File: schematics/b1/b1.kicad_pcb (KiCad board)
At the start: 2 copper layers, 0 parts

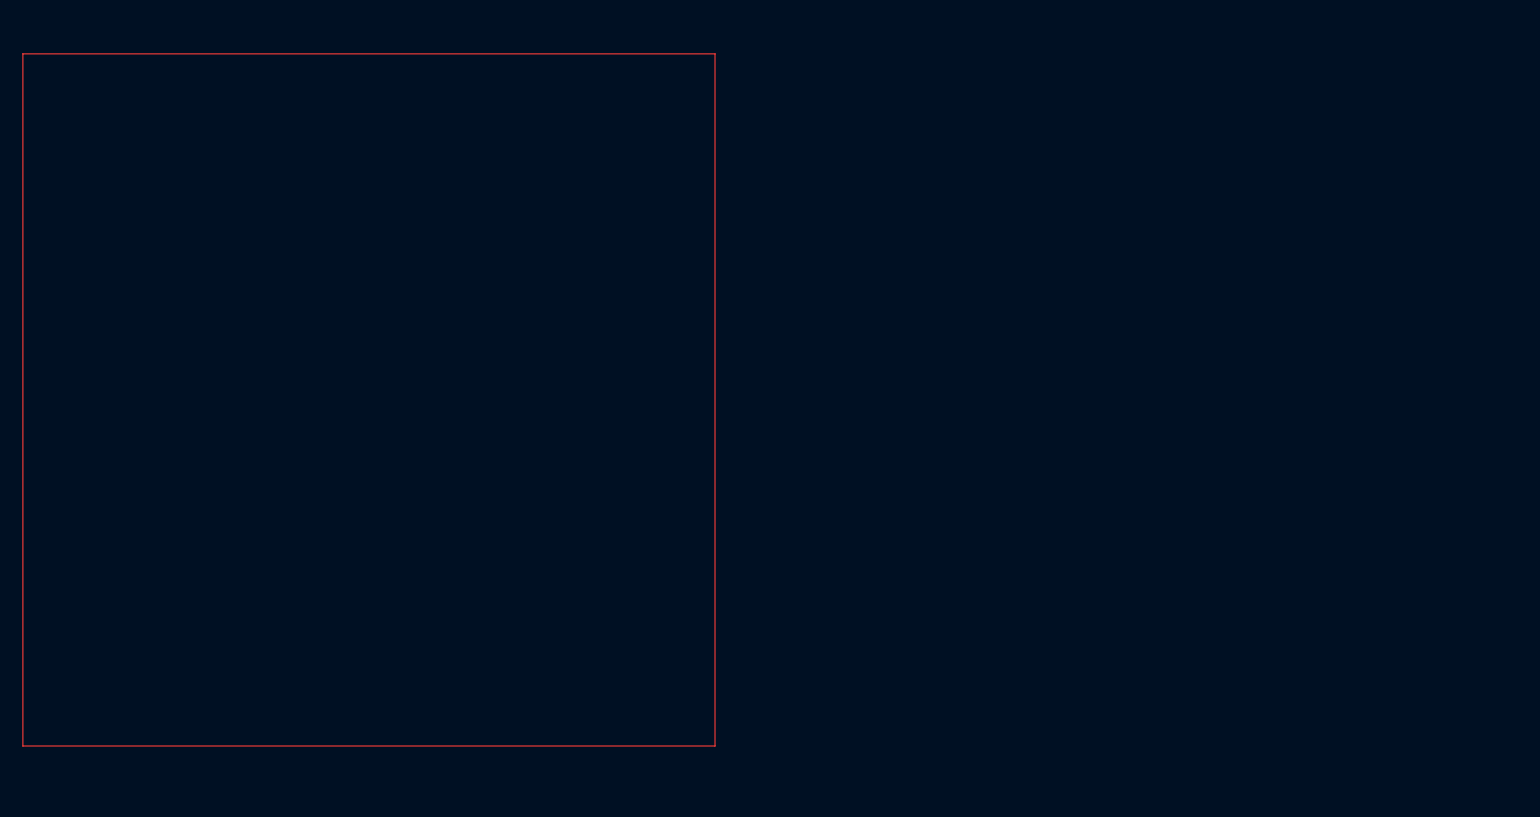
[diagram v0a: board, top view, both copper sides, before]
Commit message: Added terminal block for power in.
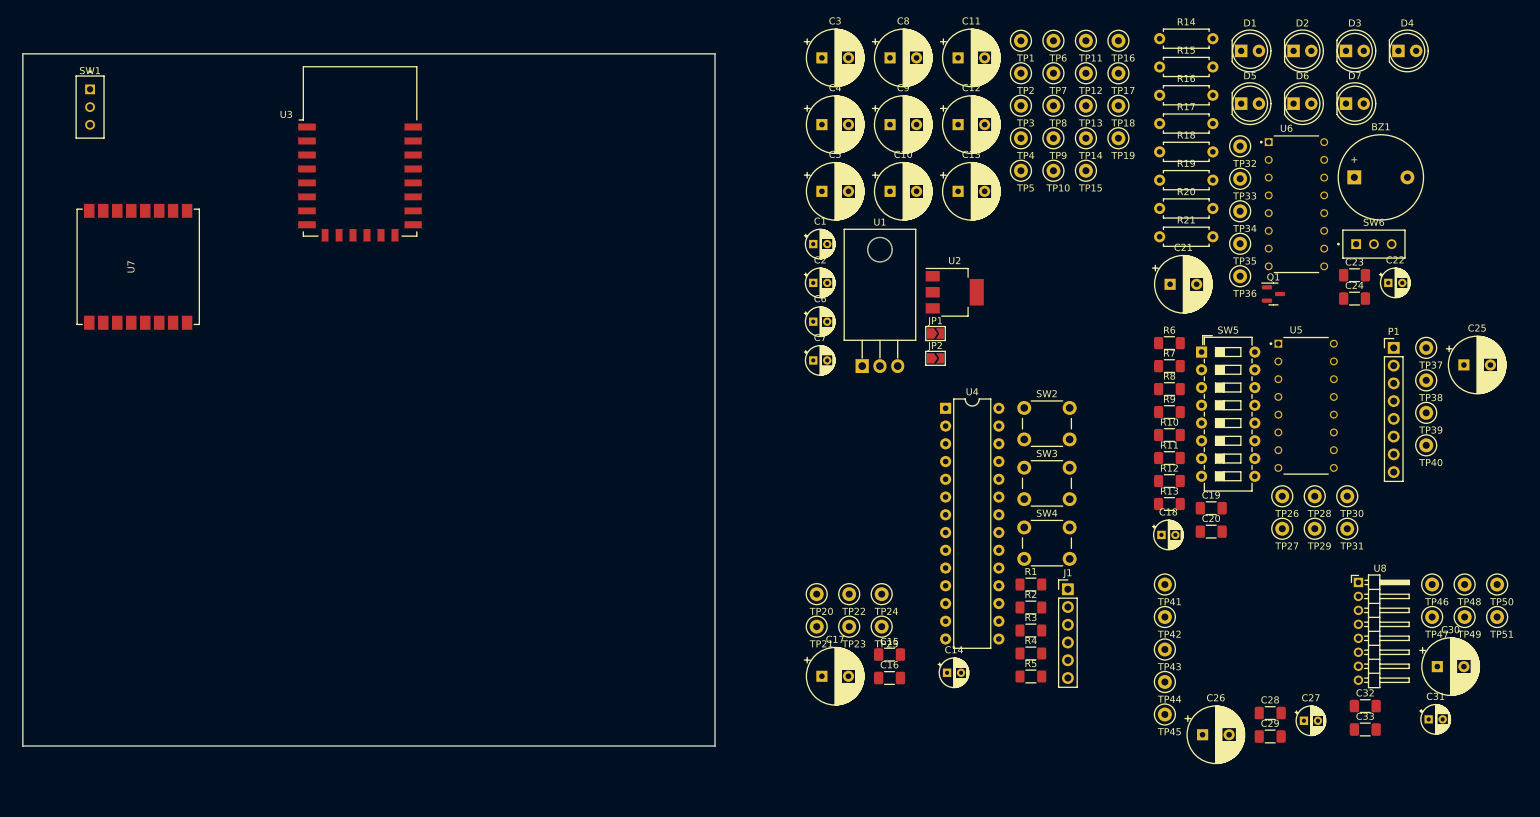
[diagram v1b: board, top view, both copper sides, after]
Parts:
- added BZ1: Buzzer, Buzzer_Beeper:Buzzer_12x9.5RM7.6, F.Cu at (285.8, 60.9)
- added C1: 10u, Capacitor_THT:CP_Radial_D4.0mm_P2.00mm, F.Cu at (208.4, 70.4)
- added C10: C, Capacitor_THT:CP_Radial_D8.0mm_P3.80mm, F.Cu at (219.4, 62.9)
- added C11: C, Capacitor_THT:CP_Radial_D8.0mm_P3.80mm, F.Cu at (229.1, 43.8)
- added C12: C, Capacitor_THT:CP_Radial_D8.0mm_P3.80mm, F.Cu at (229.1, 53.3)
- added C13: C, Capacitor_THT:CP_Radial_D8.0mm_P3.80mm, F.Cu at (229.1, 62.9)
- added C14: 10u, Capacitor_THT:CP_Radial_D4.0mm_P2.00mm, F.Cu at (227.5, 131.8)
- added C15: 1u, Capacitor_SMD:C_1206_3216Metric_Pad1.33x1.80mm_HandSolder, F.Cu at (219.3, 129.2)
- added C16: 0.1u, Capacitor_SMD:C_1206_3216Metric_Pad1.33x1.80mm_HandSolder, F.Cu at (219.3, 132.5)
- added C17: 1m, Capacitor_THT:CP_Radial_D8.0mm_P3.80mm, F.Cu at (209.6, 132.3)
- added C18: 10u, Capacitor_THT:CP_Radial_D4.0mm_P2.00mm, F.Cu at (258.2, 112.0)
- added C19: 1u, Capacitor_SMD:C_1206_3216Metric_Pad1.33x1.80mm_HandSolder, F.Cu at (265.3, 108.2)
- added C2: 10u, Capacitor_THT:CP_Radial_D4.0mm_P2.00mm, F.Cu at (208.4, 76.0)
- added C20: 0.1u, Capacitor_SMD:C_1206_3216Metric_Pad1.33x1.80mm_HandSolder, F.Cu at (265.3, 111.6)
- added C21: 470u, Capacitor_THT:CP_Radial_D8.0mm_P3.80mm, F.Cu at (259.4, 76.2)
- added C22: 10u, Capacitor_THT:CP_Radial_D4.0mm_P2.00mm, F.Cu at (290.7, 76.0)
- added C23: 1u, Capacitor_SMD:C_1206_3216Metric_Pad1.33x1.80mm_HandSolder, F.Cu at (285.8, 74.9)
- added C24: 0.1u, Capacitor_SMD:C_1206_3216Metric_Pad1.33x1.80mm_HandSolder, F.Cu at (285.8, 78.2)
- added C25: 1m, Capacitor_THT:CP_Radial_D8.0mm_P3.80mm, F.Cu at (301.5, 87.7)
- added C26: 1m, Capacitor_THT:CP_Radial_D8.0mm_P3.80mm, F.Cu at (264.1, 140.6)
- added C27: 10u, Capacitor_THT:CP_Radial_D4.0mm_P2.00mm, F.Cu at (278.6, 138.6)
- added C28: 1u, Capacitor_SMD:C_1206_3216Metric_Pad1.33x1.80mm_HandSolder, F.Cu at (273.8, 137.5)
- added C29: 0.1u, Capacitor_SMD:C_1206_3216Metric_Pad1.33x1.80mm_HandSolder, F.Cu at (273.8, 140.9)
- added C3: C, Capacitor_THT:CP_Radial_D8.0mm_P3.80mm, F.Cu at (209.6, 43.8)
- added C30: 470u, Capacitor_THT:CP_Radial_D8.0mm_P3.80mm, F.Cu at (297.7, 130.9)
- added C31: 10u, Capacitor_THT:CP_Radial_D4.0mm_P2.00mm, F.Cu at (296.4, 138.4)
- added C32: 1u, Capacitor_SMD:C_1206_3216Metric_Pad1.33x1.80mm_HandSolder, F.Cu at (287.4, 136.5)
- added C33: 0.1u, Capacitor_SMD:C_1206_3216Metric_Pad1.33x1.80mm_HandSolder, F.Cu at (287.4, 139.9)
- added C4: C, Capacitor_THT:CP_Radial_D8.0mm_P3.80mm, F.Cu at (209.6, 53.3)
- added C5: C, Capacitor_THT:CP_Radial_D8.0mm_P3.80mm, F.Cu at (209.6, 62.9)
- added C6: 10u, Capacitor_THT:CP_Radial_D4.0mm_P2.00mm, F.Cu at (208.4, 81.5)
- added C7: 10u, Capacitor_THT:CP_Radial_D4.0mm_P2.00mm, F.Cu at (208.4, 87.1)
- added C8: C, Capacitor_THT:CP_Radial_D8.0mm_P3.80mm, F.Cu at (219.4, 43.8)
- added C9: C, Capacitor_THT:CP_Radial_D8.0mm_P3.80mm, F.Cu at (219.4, 53.3)
- added D1: GREEN, LED_THT:LED_D5.0mm, F.Cu at (269.6, 42.8)
- added D2: YELLOW, LED_THT:LED_D5.0mm, F.Cu at (277.1, 42.8)
- added D3: RED, LED_THT:LED_D5.0mm, F.Cu at (284.6, 42.8)
- added D4: WHITE, LED_THT:LED_D5.0mm, F.Cu at (292.1, 42.8)
- added D5: BLUE, LED_THT:LED_D5.0mm, F.Cu at (269.6, 50.3)
- added D6: RED, LED_THT:LED_D5.0mm, F.Cu at (277.1, 50.3)
- added D7: YELLOW, LED_THT:LED_D5.0mm, F.Cu at (284.6, 50.3)
- added J1: SERIAL, Connector_PinHeader_2.54mm:PinHeader_1x06_P2.54mm_Vertical, F.Cu at (244.8, 119.8)
- added JP1: SolderJumper_2_Open, Jumper:SolderJumper-2_P1.3mm_Open_TrianglePad1.0x1.5mm, F.Cu at (225.9, 83.2)
- added JP2: SolderJumper_2_Open, Jumper:SolderJumper-2_P1.3mm_Open_TrianglePad1.0x1.5mm, F.Cu at (225.9, 86.8)
- added P1: RFID-RC522, Connector_PinHeader_2.54mm:PinHeader_1x08_P2.54mm_Vertical, F.Cu at (291.4, 85.3)
- added Q1: MMBT3904, Package_TO_SOT_SMD:SOT-23, F.Cu at (274.2, 77.5)
- added R1: 10k, Resistor_SMD:R_1206_3216Metric_Pad1.30x1.75mm_HandSolder, F.Cu at (239.5, 119.1)
- added R10: 10k, Resistor_SMD:R_1206_3216Metric_Pad1.30x1.75mm_HandSolder, F.Cu at (259.3, 97.7)
- added R11: 10k, Resistor_SMD:R_1206_3216Metric_Pad1.30x1.75mm_HandSolder, F.Cu at (259.3, 101.0)
- added R12: 10k, Resistor_SMD:R_1206_3216Metric_Pad1.30x1.75mm_HandSolder, F.Cu at (259.3, 104.3)
- added R13: 10k, Resistor_SMD:R_1206_3216Metric_Pad1.30x1.75mm_HandSolder, F.Cu at (259.3, 107.6)
- added R14: 360, Resistor_THT:R_Axial_DIN0207_L6.3mm_D2.5mm_P7.62mm_Horizontal, F.Cu at (257.9, 41.0)
- added R15: 360, Resistor_THT:R_Axial_DIN0207_L6.3mm_D2.5mm_P7.62mm_Horizontal, F.Cu at (257.9, 45.1)
- added R16: 360, Resistor_THT:R_Axial_DIN0207_L6.3mm_D2.5mm_P7.62mm_Horizontal, F.Cu at (257.9, 49.1)
- added R17: 360, Resistor_THT:R_Axial_DIN0207_L6.3mm_D2.5mm_P7.62mm_Horizontal, F.Cu at (257.9, 53.2)
- added R18: 360, Resistor_THT:R_Axial_DIN0207_L6.3mm_D2.5mm_P7.62mm_Horizontal, F.Cu at (257.9, 57.2)
- added R19: 360, Resistor_THT:R_Axial_DIN0207_L6.3mm_D2.5mm_P7.62mm_Horizontal, F.Cu at (257.9, 61.3)
- added R2: 10k, Resistor_SMD:R_1206_3216Metric_Pad1.30x1.75mm_HandSolder, F.Cu at (239.5, 122.4)
- added R20: 360, Resistor_THT:R_Axial_DIN0207_L6.3mm_D2.5mm_P7.62mm_Horizontal, F.Cu at (257.9, 65.3)
- added R21: 47, Resistor_THT:R_Axial_DIN0207_L6.3mm_D2.5mm_P7.62mm_Horizontal, F.Cu at (257.9, 69.4)
- added R3: 10k, Resistor_SMD:R_1206_3216Metric_Pad1.30x1.75mm_HandSolder, F.Cu at (239.5, 125.7)
- added R4: 10k, Resistor_SMD:R_1206_3216Metric_Pad1.30x1.75mm_HandSolder, F.Cu at (239.5, 129.0)
- added R5: 10k, Resistor_SMD:R_1206_3216Metric_Pad1.30x1.75mm_HandSolder, F.Cu at (239.5, 132.3)
- added R6: 10k, Resistor_SMD:R_1206_3216Metric_Pad1.30x1.75mm_HandSolder, F.Cu at (259.3, 84.6)
- added R7: 10k, Resistor_SMD:R_1206_3216Metric_Pad1.30x1.75mm_HandSolder, F.Cu at (259.3, 87.9)
- added R8: 10k, Resistor_SMD:R_1206_3216Metric_Pad1.30x1.75mm_HandSolder, F.Cu at (259.3, 91.2)
- added R9: 10k, Resistor_SMD:R_1206_3216Metric_Pad1.30x1.75mm_HandSolder, F.Cu at (259.3, 94.5)
- added SW1: PWR_SW, custom:SW_SPDT, F.Cu at (106.7, 50.8)
- added SW2: JUMP, Button_Switch_THT:SW_PUSH_6mm_H4.3mm, F.Cu at (238.6, 93.9)
- added SW3: RESET, Button_Switch_THT:SW_PUSH_6mm_H4.3mm, F.Cu at (238.6, 102.4)
- added SW4: FLASH, Button_Switch_THT:SW_PUSH_6mm_H4.3mm, F.Cu at (238.6, 111.0)
- added SW5: SW_DIP_x08, Button_Switch_THT:SW_DIP_SPSTx08_Slide_6.7x21.88mm_W7.62mm_P2.54mm_LowProfile, F.Cu at (263.9, 85.9)
- added SW6: SW_SPDT, custom:SW_SPDT, F.Cu at (288.6, 68.6)
- added TP1: TestPoint, TestPoint:TestPoint_Loop_D2.50mm_Drill1.0mm, F.Cu at (238.1, 41.3)
- added TP10: TestPoint, TestPoint:TestPoint_Loop_D2.50mm_Drill1.0mm, F.Cu at (242.7, 59.9)
- added TP11: TestPoint, TestPoint:TestPoint_Loop_D2.50mm_Drill1.0mm, F.Cu at (247.4, 41.3)
- added TP12: TestPoint, TestPoint:TestPoint_Loop_D2.50mm_Drill1.0mm, F.Cu at (247.4, 46.0)
- added TP13: TestPoint, TestPoint:TestPoint_Loop_D2.50mm_Drill1.0mm, F.Cu at (247.4, 50.6)
- added TP14: TestPoint, TestPoint:TestPoint_Loop_D2.50mm_Drill1.0mm, F.Cu at (247.4, 55.3)
- added TP15: TestPoint, TestPoint:TestPoint_Loop_D2.50mm_Drill1.0mm, F.Cu at (247.4, 59.9)
- added TP16: TestPoint, TestPoint:TestPoint_Loop_D2.50mm_Drill1.0mm, F.Cu at (252.0, 41.3)
- added TP17: TestPoint, TestPoint:TestPoint_Loop_D2.50mm_Drill1.0mm, F.Cu at (252.0, 46.0)
- added TP18: TestPoint, TestPoint:TestPoint_Loop_D2.50mm_Drill1.0mm, F.Cu at (252.0, 50.6)
- added TP19: TestPoint, TestPoint:TestPoint_Loop_D2.50mm_Drill1.0mm, F.Cu at (252.0, 55.3)
- added TP2: TestPoint, TestPoint:TestPoint_Loop_D2.50mm_Drill1.0mm, F.Cu at (238.1, 46.0)
- added TP20: TestPoint, TestPoint:TestPoint_Loop_D2.50mm_Drill1.0mm, F.Cu at (208.9, 120.5)
- added TP21: TestPoint, TestPoint:TestPoint_Loop_D2.50mm_Drill1.0mm, F.Cu at (208.9, 125.2)
- added TP22: TestPoint, TestPoint:TestPoint_Loop_D2.50mm_Drill1.0mm, F.Cu at (213.5, 120.5)
- added TP23: TestPoint, TestPoint:TestPoint_Loop_D2.50mm_Drill1.0mm, F.Cu at (213.5, 125.2)
- added TP24: TestPoint, TestPoint:TestPoint_Loop_D2.50mm_Drill1.0mm, F.Cu at (218.2, 120.5)
- added TP25: TestPoint, TestPoint:TestPoint_Loop_D2.50mm_Drill1.0mm, F.Cu at (218.2, 125.2)
- added TP26: TestPoint, TestPoint:TestPoint_Loop_D2.50mm_Drill1.0mm, F.Cu at (275.5, 106.5)
- added TP27: TestPoint, TestPoint:TestPoint_Loop_D2.50mm_Drill1.0mm, F.Cu at (275.5, 111.2)
- added TP28: TestPoint, TestPoint:TestPoint_Loop_D2.50mm_Drill1.0mm, F.Cu at (280.1, 106.5)
- added TP29: TestPoint, TestPoint:TestPoint_Loop_D2.50mm_Drill1.0mm, F.Cu at (280.1, 111.2)
- added TP3: TestPoint, TestPoint:TestPoint_Loop_D2.50mm_Drill1.0mm, F.Cu at (238.1, 50.6)
- added TP30: TestPoint, TestPoint:TestPoint_Loop_D2.50mm_Drill1.0mm, F.Cu at (284.8, 106.5)
- added TP31: TestPoint, TestPoint:TestPoint_Loop_D2.50mm_Drill1.0mm, F.Cu at (284.8, 111.2)
- added TP32: TestPoint, TestPoint:TestPoint_Loop_D2.50mm_Drill1.0mm, F.Cu at (269.5, 56.4)
- added TP33: TestPoint, TestPoint:TestPoint_Loop_D2.50mm_Drill1.0mm, F.Cu at (269.5, 61.1)
- added TP34: TestPoint, TestPoint:TestPoint_Loop_D2.50mm_Drill1.0mm, F.Cu at (269.5, 65.7)
- added TP35: TestPoint, TestPoint:TestPoint_Loop_D2.50mm_Drill1.0mm, F.Cu at (269.5, 70.4)
- added TP36: TestPoint, TestPoint:TestPoint_Loop_D2.50mm_Drill1.0mm, F.Cu at (269.5, 75.0)
- added TP37: TestPoint, TestPoint:TestPoint_Loop_D2.50mm_Drill1.0mm, F.Cu at (296.1, 85.3)
- added TP38: TestPoint, TestPoint:TestPoint_Loop_D2.50mm_Drill1.0mm, F.Cu at (296.1, 89.9)
- added TP39: TestPoint, TestPoint:TestPoint_Loop_D2.50mm_Drill1.0mm, F.Cu at (296.1, 94.6)
- added TP4: TestPoint, TestPoint:TestPoint_Loop_D2.50mm_Drill1.0mm, F.Cu at (238.1, 55.3)
- added TP40: TestPoint, TestPoint:TestPoint_Loop_D2.50mm_Drill1.0mm, F.Cu at (296.1, 99.2)
- added TP41: TestPoint, TestPoint:TestPoint_Loop_D2.50mm_Drill1.0mm, F.Cu at (258.7, 119.1)
- added TP42: TestPoint, TestPoint:TestPoint_Loop_D2.50mm_Drill1.0mm, F.Cu at (258.7, 123.8)
- added TP43: TestPoint, TestPoint:TestPoint_Loop_D2.50mm_Drill1.0mm, F.Cu at (258.7, 128.4)
- added TP44: TestPoint, TestPoint:TestPoint_Loop_D2.50mm_Drill1.0mm, F.Cu at (258.7, 133.1)
- added TP45: TestPoint, TestPoint:TestPoint_Loop_D2.50mm_Drill1.0mm, F.Cu at (258.7, 137.7)
- added TP46: TestPoint, TestPoint:TestPoint_Loop_D2.50mm_Drill1.0mm, F.Cu at (296.9, 119.1)
- added TP47: TestPoint, TestPoint:TestPoint_Loop_D2.50mm_Drill1.0mm, F.Cu at (296.9, 123.8)
- added TP48: TestPoint, TestPoint:TestPoint_Loop_D2.50mm_Drill1.0mm, F.Cu at (301.6, 119.1)
- added TP49: TestPoint, TestPoint:TestPoint_Loop_D2.50mm_Drill1.0mm, F.Cu at (301.6, 123.8)
- added TP5: TestPoint, TestPoint:TestPoint_Loop_D2.50mm_Drill1.0mm, F.Cu at (238.1, 59.9)
- added TP50: TestPoint, TestPoint:TestPoint_Loop_D2.50mm_Drill1.0mm, F.Cu at (306.2, 119.1)
- added TP51: TestPoint, TestPoint:TestPoint_Loop_D2.50mm_Drill1.0mm, F.Cu at (306.2, 123.8)
- added TP6: TestPoint, TestPoint:TestPoint_Loop_D2.50mm_Drill1.0mm, F.Cu at (242.7, 41.3)
- added TP7: TestPoint, TestPoint:TestPoint_Loop_D2.50mm_Drill1.0mm, F.Cu at (242.7, 46.0)
- added TP8: TestPoint, TestPoint:TestPoint_Loop_D2.50mm_Drill1.0mm, F.Cu at (242.7, 50.6)
- added TP9: TestPoint, TestPoint:TestPoint_Loop_D2.50mm_Drill1.0mm, F.Cu at (242.7, 55.3)
- added U1: L7805, Package_TO_SOT_THT:TO-220-3_Horizontal_TabDown, F.Cu at (215.4, 87.9)
- added U2: AMS1117-3.3, Package_TO_SOT_SMD:SOT-223-3_TabPin2, F.Cu at (228.6, 77.3)
- added U3: ESP-12F, RF_Module:ESP-12E, F.Cu at (143.5, 57.1)
- added U4: MCP23017_SP, Package_DIP:DIP-28_W7.62mm, F.Cu at (227.3, 93.9)
- added U5: 74HC165, SN74HC595N:DIP794W45P254L1969H508Q16, F.Cu at (278.9, 93.6)
- added U6: 74HC595, SN74HC595N:DIP794W45P254L1969H508Q16, F.Cu at (277.5, 64.7)
- added U7: Ai-Thinker-Ra-02, RF_Module:Ai-Thinker-Ra-01-LoRa, F.Cu at (111.8, 73.7)
- added U8: Display, Connector_PinHeader_2.00mm:PinHeader_1x08_P2.00mm_Horizontal, F.Cu at (286.4, 118.8)
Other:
- board outline added: 99.1 x 99.1 mm

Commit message: Routed some traces.
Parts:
- added J2: POWER, TerminalBlock:TerminalBlock_bornier-2_P5.08mm, F.Cu at (99.4, 47.0)
- C10, C11, C12, C13, C3, C4, C5, C8, C9: footprint Capacitor_THT:CP_Radial_D8.0mm_P3.80mm -> Capacitor_THT:CP_Radial_D4.0mm_P2.00mm
- moved P1 195.1 mm to (98.6, 114.4)
- moved U8 182.5 mm to (104.2, 107.8), turned to 180 degrees
- moved D4 151.2 mm to (175.6, 139.2), turned to 90 degrees
- moved D7 145.9 mm to (168.9, 139.2), turned to 90 degrees
- moved D3 141.2 mm to (175.6, 132.6), turned to 90 degrees
- moved U5 137.6 mm to (148.6, 49.5), turned to -90 degrees
- moved D6 135.9 mm to (168.9, 132.6), turned to 90 degrees
- moved SW6 132.6 mm to (161.1, 105.2), turned to 180 degrees
- moved D2 131.2 mm to (175.6, 126.0), turned to 90 degrees
- moved D5 126.0 mm to (168.9, 126.0), turned to 90 degrees
- moved SW5 124.7 mm to (139.7, 74.9), turned to 90 degrees
- moved BZ1 124.1 mm to (169.2, 103.4)
- moved C20 122.8 mm to (155.9, 55.9), turned to 180 degrees
- moved D1 121.3 mm to (175.6, 119.4), turned to 90 degrees
- moved C19 120.2 mm to (155.9, 58.4), turned to 180 degrees
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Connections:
- SW1 pad 2: +BATT -> Net-(J2-Pin_1)
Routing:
- net /5V: track 0.00 -> 67.4 mm
- net /VRAW: track 0.00 -> 51.7 mm
- net /Wi-Fi and MCU/GPIO0: track 0.00 -> 23.5 mm
- net GND: track 0.00 -> 13.0 mm
- net Net-(U3-~{RST}): track 0.00 -> 13.0 mm
- net Net-(J2-Pin_1): track 0.00 -> 12.8 mm
- net /3V3: track 0.00 -> 11.8 mm
- net Net-(J1-TX): track 0.00 -> 7.98 mm
- net Net-(J1-RX): track 0.00 -> 7.43 mm
- net Net-(BZ1-+): track 0.00 -> 5.07 mm
- net Net-(SW6-B): track 0.00 -> 4.45 mm
- net Net-(Q1-B): track 0.00 -> 3.47 mm
- net /Status Block/BUZZ: track 0.00 -> 3.42 mm
- net /Wi-Fi and MCU/GPIO15: track 0.00 -> 3.38 mm
- net Net-(U3-EN): track 0.00 -> 3.35 mm
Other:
- board size 99.1 x 99.1 mm -> 100 x 100 mm
- board text added: "DANGER JUMPER"
- board text added: "FLASH"
- board text added: "OFF"
- board text added: "ON"
- board text added: "RST"

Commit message: Routed traces.
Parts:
- removed C11, C12, C13, C3, C4: C, Capacitor_THT:CP_Radial_D4.0mm_P2.00mm
- removed TP15, TP16, TP17, TP19, TP31, TP8: TestPoint, TestPoint:TestPoint_Loop_D2.50mm_Drill1.0mm
- added H1: MountingHole, MountingHole:MountingHole_2.2mm_M2, F.Cu at (121.9, 48.5)
- added H2: MountingHole, MountingHole:MountingHole_2.2mm_M2, F.Cu at (186.2, 46.1)
- added H3: MountingHole, MountingHole:MountingHole_2.2mm_M2, F.Cu at (163.7, 131.1)
- added H4: MountingHole, MountingHole:MountingHole_2.2mm_M2, F.Cu at (154.2, 81.4)
- C28, C29, JP1, R3, R5: moved to B.Cu
- D1: value GREEN -> WHITE
- D3: value RED -> GREEN
- D4: value WHITE -> RED
- moved C27 182.0 mm to (99.7, 118.7), turned to 180 degrees
- moved TP49 178.2 mm to (126.5, 103.8)
- moved TP51 177.9 mm to (129.7, 129.2)
- moved C29 173.1 mm to (102.6, 131.6), turned to 180 degrees
- moved C28 172.7 mm to (102.6, 134.0), turned to 180 degrees
- moved C26 170.9 mm to (98.4, 109.6)
- moved TP26 169.6 mm to (108.0, 95.8)
- moved TP30 169.5 mm to (117.9, 91.4)
- moved TP50 169.3 mm to (138.4, 115.7)
- moved TP48 167.4 mm to (136.3, 108.8)
- moved TP47 164.6 mm to (134.2, 115.7)
- moved TP27 162.4 mm to (115.6, 97.2)
- moved TP28 160.1 mm to (122.4, 93.7)
- moved TP44 159.3 mm to (102.2, 116.2)
- moved C25 155.4 mm to (153.2, 135.4), turned to 90 degrees
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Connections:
- C5 pad 1: /5V -> /3V3
- R21 pad 1: Net-(U6-QH) -> Net-(U6-QA)
- U6 pad 1: Net-(D2-A) -> Net-(D1-A)
- U6 pad 15: Net-(D1-A) -> Net-(U6-QA)
- U6 pad 2: Net-(D3-A) -> Net-(D2-A)
- U6 pad 3: Net-(D4-A) -> Net-(D3-A)
- U6 pad 4: Net-(D5-A) -> Net-(D4-A)
- U6 pad 5: Net-(D6-A) -> Net-(D5-A)
- U6 pad 6: Net-(D7-A) -> Net-(D6-A)
- U6 pad 7: Net-(U6-QH) -> Net-(D7-A)
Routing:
- net /3V3: track 11.8 -> 717.1 mm, vias 0 -> 2
- net /MOSI: track 0.00 -> 207.1 mm, vias 0 -> 1
- net /SCLK: track 0.00 -> 193.0 mm, vias 0 -> 3
- net /MISO: track 0.00 -> 180.7 mm, vias 0 -> 4
- net /LoRa/DIO0: track 0.00 -> 86.3 mm, vias 0 -> 1
- net /Status Block/BUZZ: track 3.42 -> 71.5 mm, vias 0 -> 2
- net /Scanner/~{SS}: track 0.00 -> 65.5 mm
- net /LoRa/~{RESET}: track 0.00 -> 61.5 mm, vias 0 -> 1
- net /Scanner/RST: track 0.00 -> 59.9 mm, vias 0 -> 1
- net Net-(U3-GPIO5): track 0.00 -> 56.2 mm, vias 0 -> 1
- net Net-(U3-GPIO4): track 0.00 -> 53.1 mm, vias 0 -> 1
- net /E-Paper/DC: track 0.00 -> 48.8 mm, vias 0 -> 2
- net /Status Block/RCLK: track 0.00 -> 47.7 mm
- net /LoRa/~{NSS}: track 0.00 -> 44.9 mm
- net /E-Paper/~{RST}: track 0.00 -> 44.8 mm, vias 0 -> 2
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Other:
- board text added: "+"
- board text added: "-"
- board text added: "FLSH"
- board text added: "ID SWITCHES"
- board text removed: "FLASH"

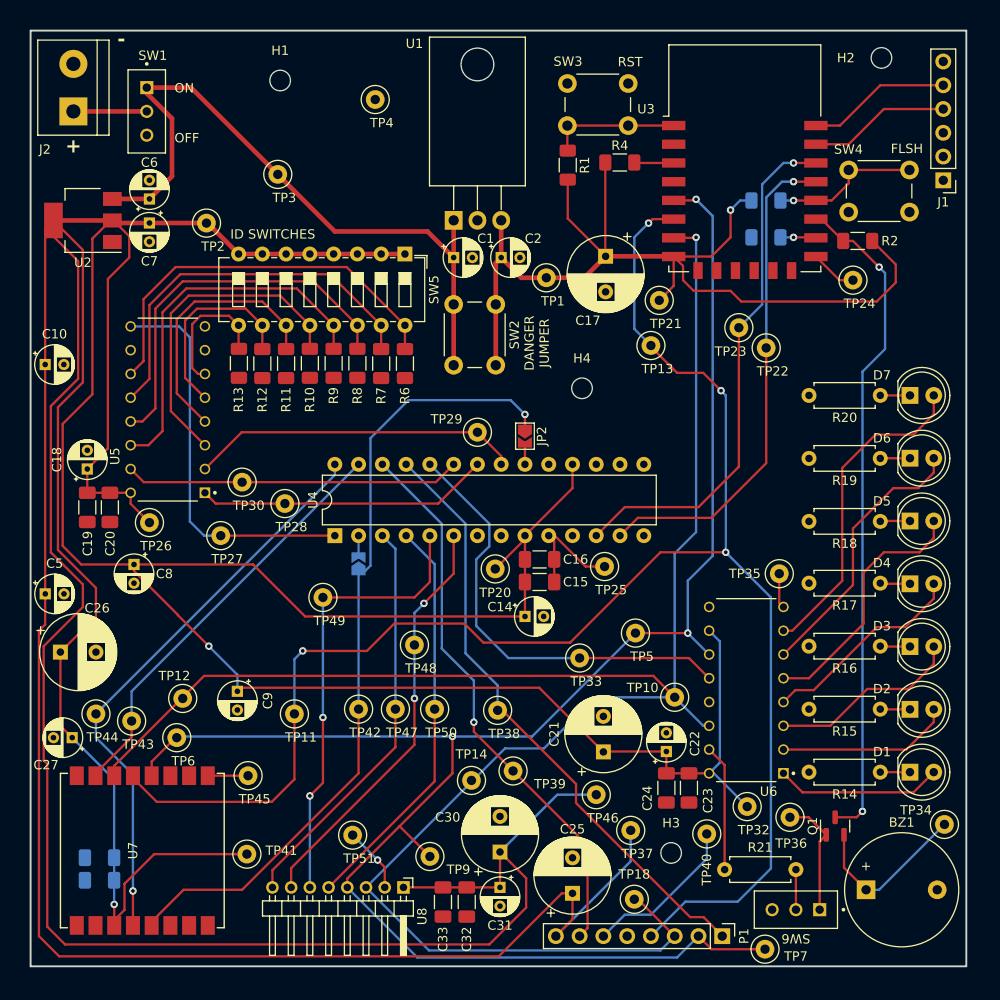
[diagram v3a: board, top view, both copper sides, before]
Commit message: Added a ground plane to the PCB.
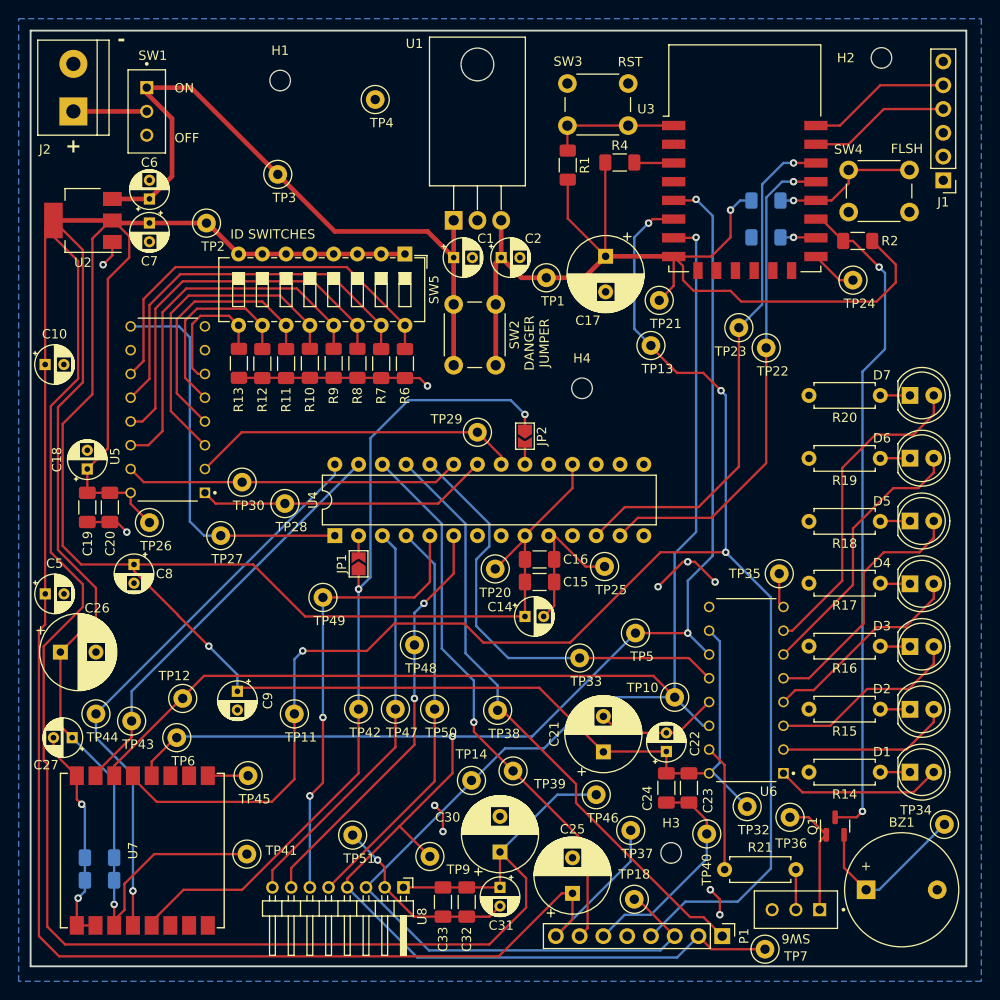
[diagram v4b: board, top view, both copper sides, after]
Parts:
- JP1: moved to F.Cu
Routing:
- net GND: track 49.7 -> 154.1 mm, vias 1 -> 13
- net /LoRa/DIO0: track 86.3 -> 87.8 mm, vias 1 -> 2
- added copper zone on B.Cu, net GND

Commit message: Created gerber files.
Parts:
- moved H1 12.4 mm to (128.9, 58.8)
- moved TP4 8.80 mm to (135.1, 58.8)
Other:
- board text added: "Badger One B1r1 by shawnd.xyz gobadger.me"
- board text added: "FLASH"
- board text added: "INT"
- board text added: "JLCJLCJLCJLC"
- board text added: "RESET"
- board text removed: "FLSH"
- board text removed: "RST"
